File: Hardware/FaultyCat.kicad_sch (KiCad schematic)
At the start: 90 parts, among them J1 Antenna, J2 BG306-02-A-2-0400-L-G, J3 Conn_01x10, J4 Header 2, J5 Header 4, J6 Input Power:2x AA Battery, P1 USB_C_Plug_USB2.0, Q1 AO3422, Q1 DMG3415U-7, Q2 AO3422, Q3 LDA111STR, Q4 RGT16BM65DTL, Q7 IRLML2502, Q8 IRF7807PBF, SW1 TL3305AF260QG, SW2 ON, SW3 TL3305AF260QG, SW4 RESET, SW5 BOOT, SW6 TL3305AF260QG, SW7 SW_SP3T, T1 ATB322524, T2 ATB322524, U1 AP2112K-3.3, U2 W25Q16JV, U3 RP2040, U4 TXB0108PW, U5 TLV75718PDBV, X1 BU-SMA, X2 BU-SMA, Y1 12Mhz

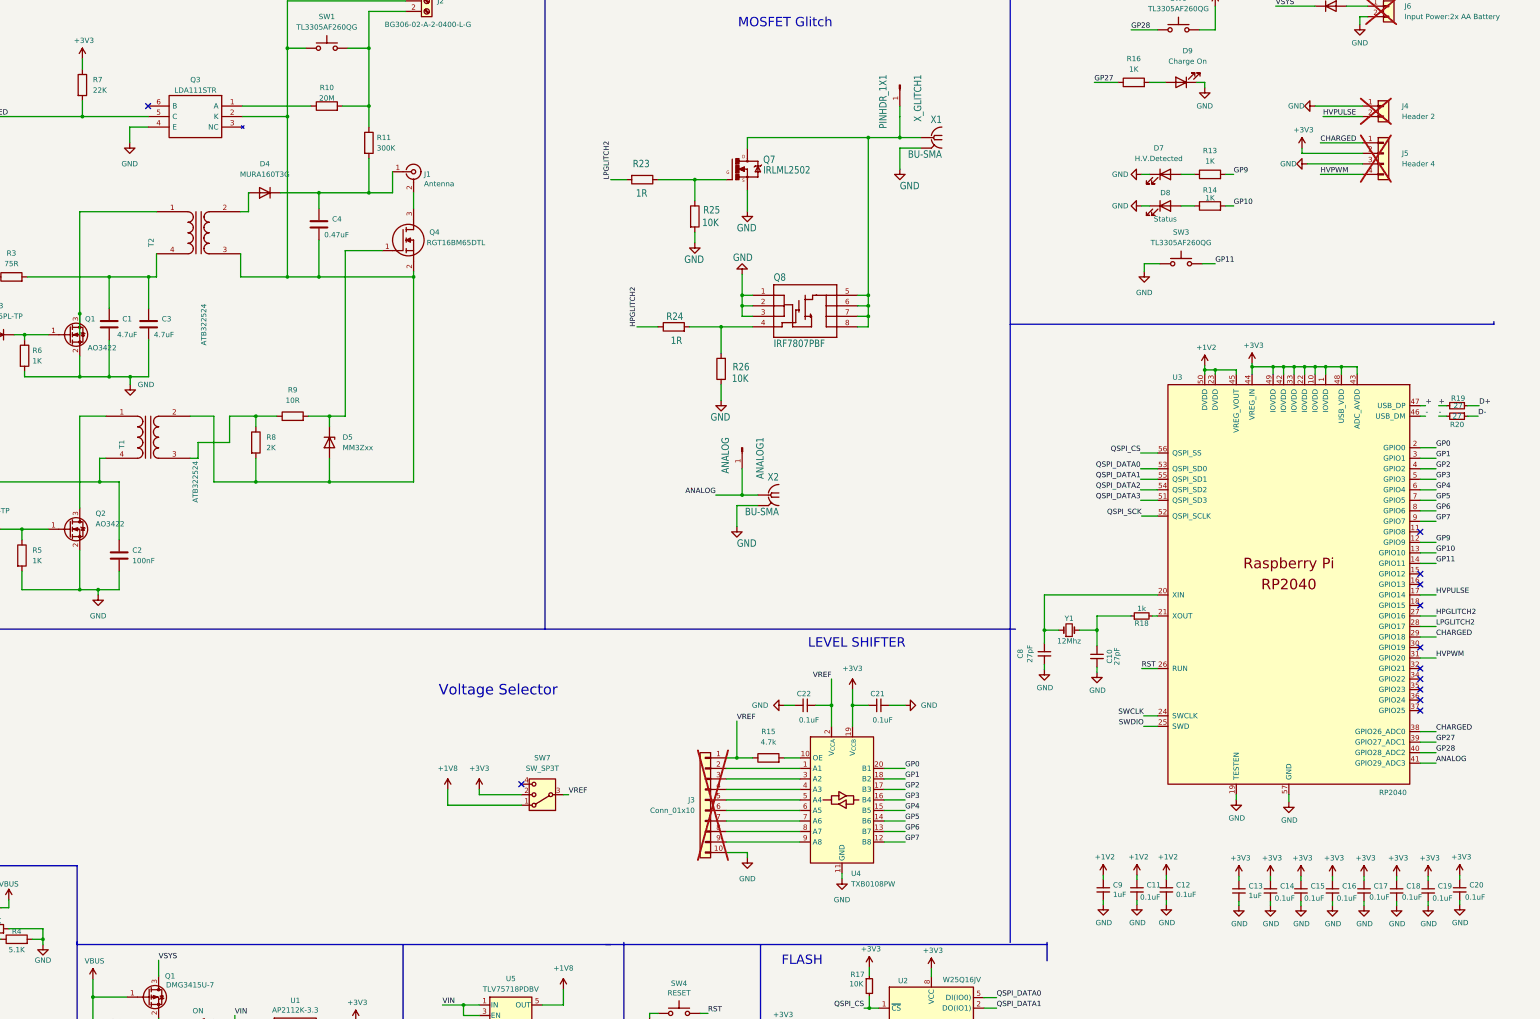
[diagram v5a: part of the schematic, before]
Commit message: feat(hw): add trigger pin and level shifter
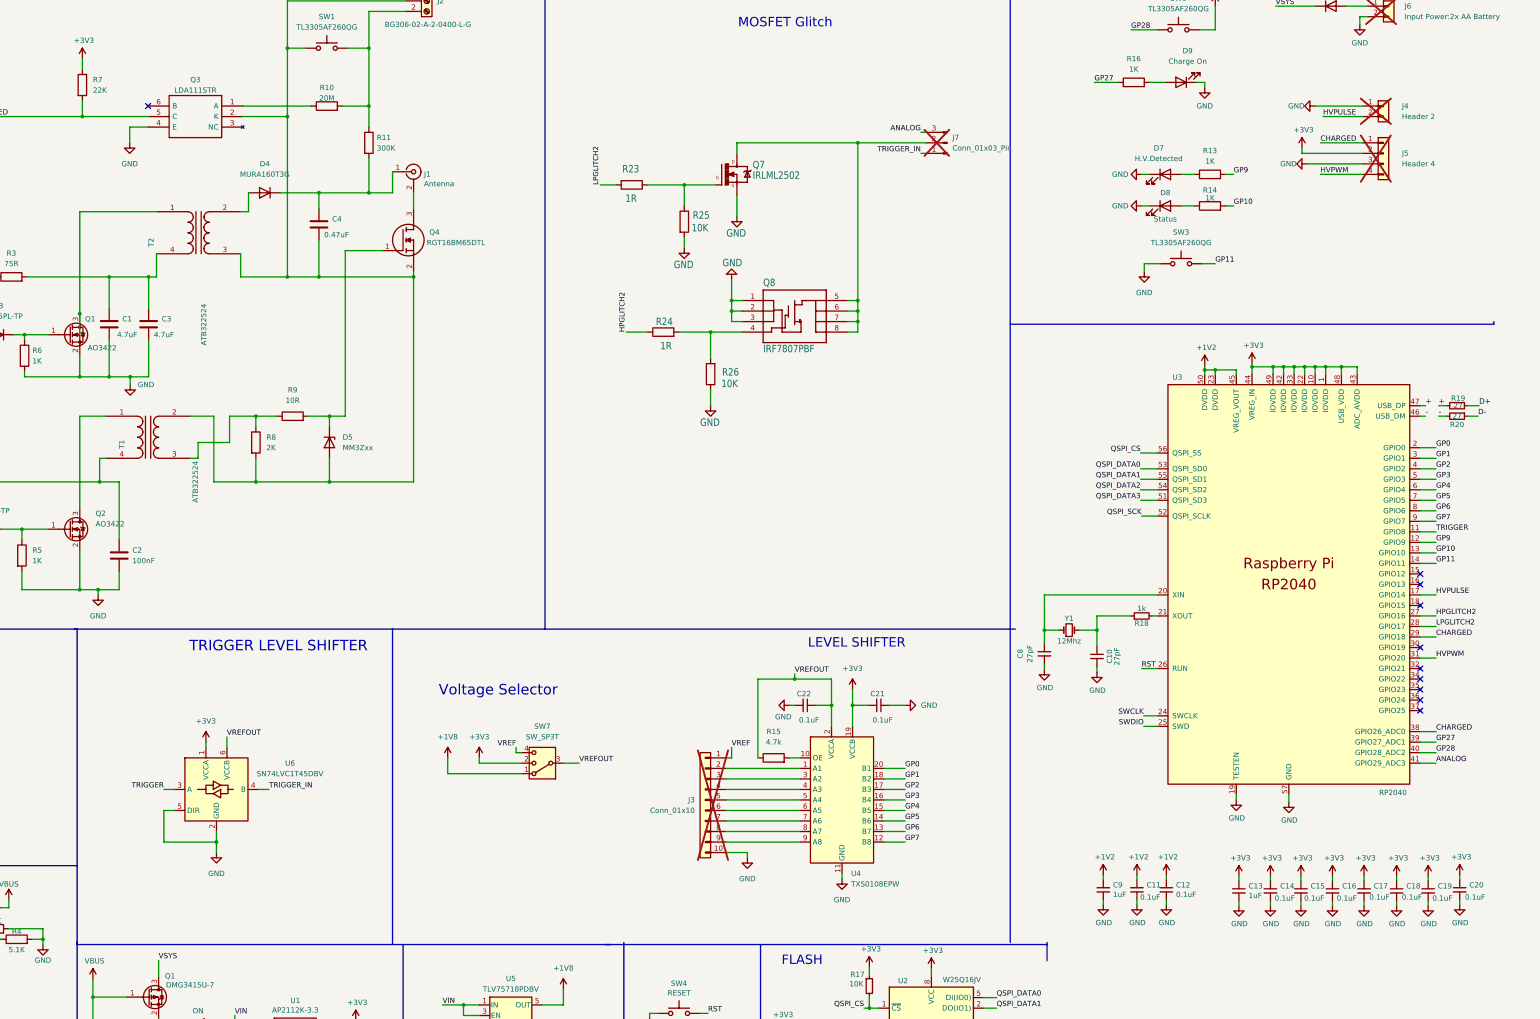
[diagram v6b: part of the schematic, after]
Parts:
- removed ANALOG1: ANALOG, Connector_PinHeader_2.54mm:PinHeader_1x01_P2.54mm_Vertical, symbol Connector:Conn_01x01_Pin
- removed U4: TXB0108PW, Package_SO:TSSOP-20_4.4x6.5mm_P0.65mm, symbol Logic_LevelTranslator:TXB0108PW
- removed X1, X2: BU-SMA, BuggyCat:SMA-KE901, symbol pico-glitcher:BU-SMA-V
- removed X_GLITCH1: PINHDR_1X1, Connector_PinHeader_2.54mm:PinHeader_1x01_P2.54mm_Vertical, symbol Connector:Conn_01x01_Pin
- added J7: Conn_01x03_Pin, Connector_PinHeader_2.54mm:PinHeader_1x03_P2.54mm_Vertical, symbol Connector:Conn_01x03_Pin
- added U4: TXS0108EPW, Package_SO:TSSOP-20_4.4x6.5mm_P0.65mm, symbol Logic_LevelTranslator:TXS0108EPW
- added U6: SN74LVC1T45DBV, Package_TO_SOT_SMD:SOT-23-6, symbol Logic_LevelTranslator:SN74LVC1T45DBV
- SW7: LCSC# (none) -> C2681567
- U3: LCSC# (none) -> C2040
- U5: LCSC# (none) -> C507270
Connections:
- net +3V3: now also U4.19 (VCCB), U6.1 (VCCA)
- net ANALOG: now also J7.3 (Pin_3)
- net GND: now also U4.11 (GND), U6.2 (GND), U6.5 (DIR)
- net GP0: now also U4.20 (B1)
- net GP1: now also U4.18 (B2)
- net GP2: now also U4.17 (B3)
- net GP3: now also U4.16 (B4)
- net GP4: now also U4.15 (B5)
- net GP5: now also U4.14 (B6)
- net GP6: now also U4.13 (B7)
- net GP7: now also U4.12 (B8)
- net VREF: now also SW7.4; no longer C22.1, R15.1, SW7.3
- net TRIGGER: now reaches U3.11 (GPIO8)
- net TRIGGER: now also U6.3 (A)
- net at J3.2 (Pin_2): now also U4.1 (A1)
- net at J3.3 (Pin_3): now also U4.3 (A2)
- net at J3.4 (Pin_4): now also U4.4 (A3)
- net at J3.5 (Pin_5): now also U4.5 (A4)
- net at J3.6 (Pin_6): now also U4.6 (A5)
- net at J3.7 (Pin_7): now also U4.7 (A6)
- net at J3.8 (Pin_8): now also U4.8 (A7)
- net at J3.9 (Pin_9): now also U4.9 (A8)
- net at Q7.3 (D), Q8.5 (D@4), Q8.6 (D@3)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: now also J7.2 (Pin_2)
- net at R15.2: now also U4.10 (OE)
- new net TRIGGER_IN: J7.1 (Pin_1), U6.4 (B)
- new net VREFOUT: C22.1, R15.1, SW7.3, U4.2 (VCCA), U6.6 (VCCB)
- no-connect marks 13 -> 11
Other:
- note added: "TRIGGER LEVEL SHIFTER"
- moved on the sheet: Q7, Q8, R15, R23, R24, R25, R26, SW7

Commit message: feat(hw): change position of pins
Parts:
- removed J7: Conn_01x03_Pin, Connector_PinHeader_2.54mm:PinHeader_1x03_P2.54mm_Vertical, symbol Connector:Conn_01x03_Pin
- added J10: TRIGGER_VREF, Connector_PinSocket_2.54mm:PinSocket_1x02_P2.54mm_Vertical, symbol Connector:Conn_01x02_Pin
- added J7: GLITCHER_EN, Connector_PinSocket_2.54mm:PinSocket_1x02_P2.54mm_Vertical, symbol Connector:Conn_01x02_Pin
- added J8: ANALOG_PINS, Connector_PinSocket_2.54mm:PinSocket_1x02_P2.54mm_Vertical, symbol Connector:Conn_01x02_Pin
- added J9: TRIGGER_IN, Connector_PinSocket_2.54mm:PinSocket_1x02_P2.54mm_Vertical, symbol Connector:Conn_01x02_Pin
- added R21, R22: R, Resistor_SMD:R_0603_1608Metric, symbol Device:R
- J3: now fitted
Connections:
- net +3V3: now also R22.2
- net ANALOG: now also J8.1 (Pin_1), J8.2 (Pin_2)
- net GND: now also R21.1; no longer U6.5 (DIR)
- net TRIGGER_IN: now also J9.1 (Pin_1), J9.2 (Pin_2)
- net VREFOUT: no longer U6.6 (VCCB)
- net GLITCHER: now reaches Q7.3 (D), Q8.5 (D@4), Q8.6 (D@3), Q8.7 (D@2), Q8.8 (D@1)
- net GLITCHER: now also J7.1 (Pin_1), J7.2 (Pin_2)
- new net: R21.2, R22.1, U6.5 (DIR)
- new net TRIGGER_VREF: J10.1 (Pin_1), J10.2 (Pin_2), U6.6 (VCCB)
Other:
- note added: "PIN CONNECTORS"
